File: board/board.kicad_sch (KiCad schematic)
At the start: 13 parts

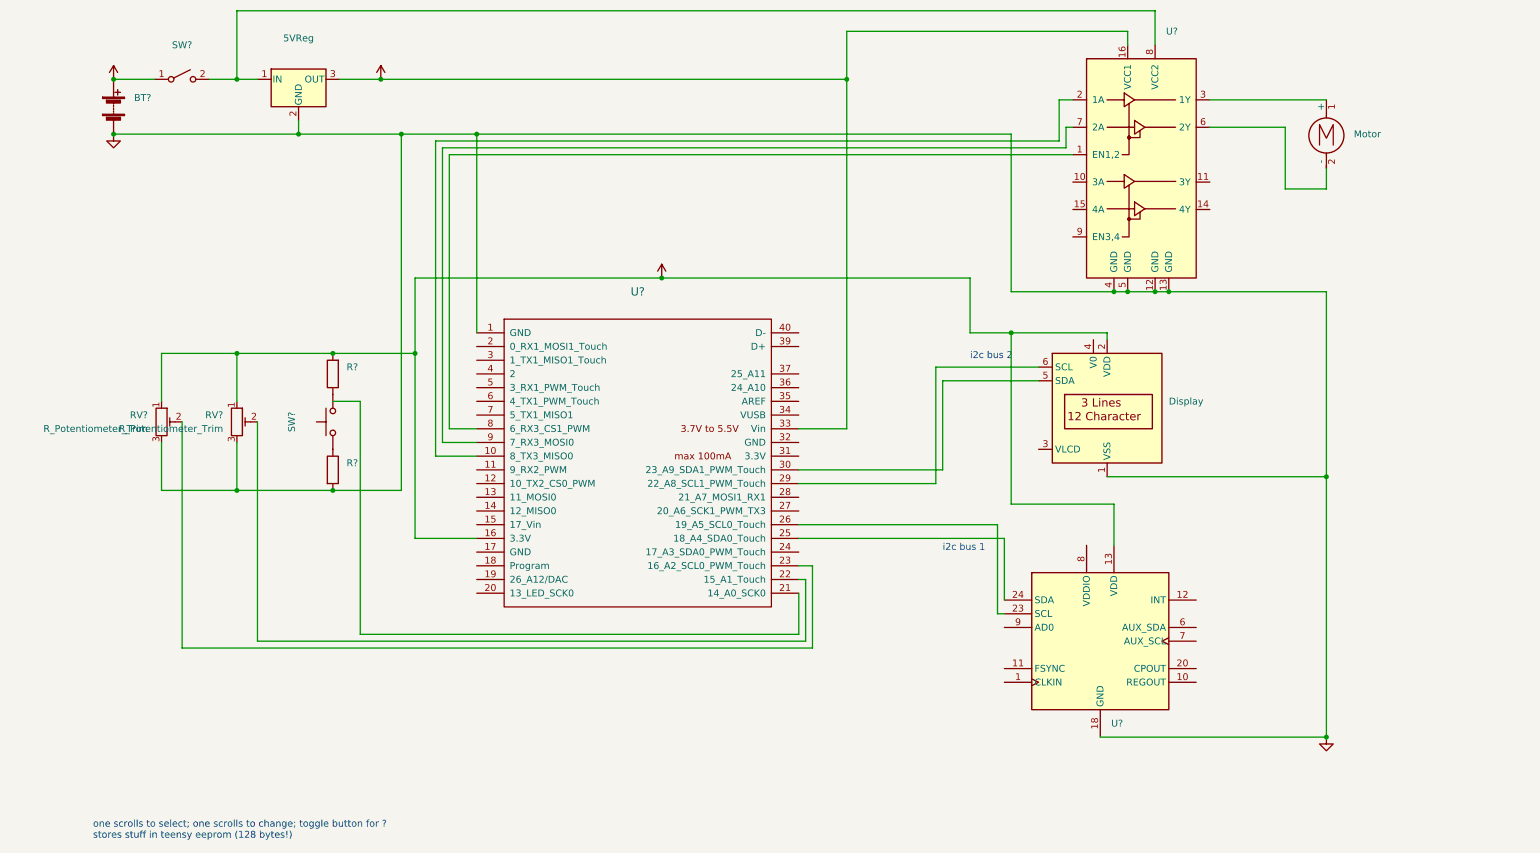
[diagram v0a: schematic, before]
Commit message: Schematic update to stepper
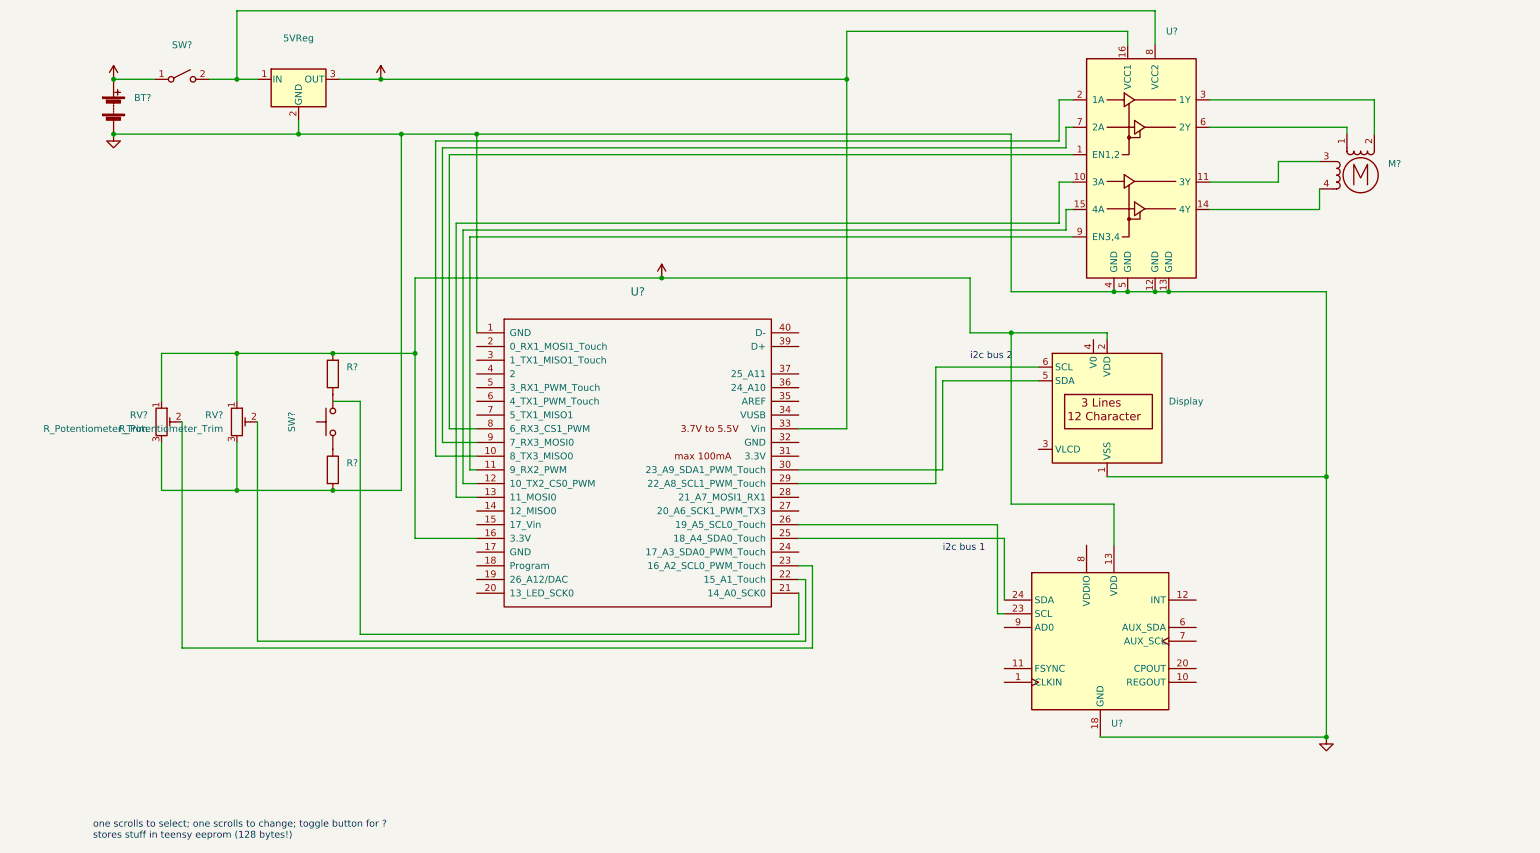
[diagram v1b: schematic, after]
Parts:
- removed Motor: (no value), symbol Motor:Motor_DC
- added M?: (no value), symbol Motor:Stepper_Motor_bipolar
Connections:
- net at U?.3 (1Y): now also M?.2 (-)
- net at U?.6 (2Y): now also M?.1
- net at U?.11 (9_RX2_PWM): now also U?.9 (EN3,4)
- net at U?.12 (10_TX2_CS0_PWM): now also U?.15 (4A)
- net at U?.13 (11_MOSI0): now also U?.10 (3A)
- net at U?.11 (3Y): now also M?.3
- net at U?.14 (4Y): now also M?.4
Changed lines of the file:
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@@
+    (stroke (width 0) (type default) (color 0 0 0 0))
+  )
+  (wire (pts (xy 256.54 33.02) (xy 256.54 39.37))
+    (stroke (width 0) (type default) (color 0 0 0 0))
+  )
+  (wire (pts (xy 226.06 38.1) (xy 251.46 38.1))
     (stroke (width 0) (type default) (color 0 0 0 0))
   )
@@
     (stroke (width 0) (type default) (color 0 0 0 0))
   )
-  (wire (pts (xy 226.06 33.02) (xy 247.65 33.02))
-    (stroke (width 0) (type default) (color 0 0 0 0))
-  )
   (wire (pts (xy 35.56 134.62) (xy 152.4 134.62))
     (stroke (width 0) (type default) (color 0 0 0 0))
   )
+  (wire (pts (xy 251.46 38.1) (xy 251.46 39.37))
+    (stroke (width 0) (type default) (color 0 0 0 0))
+  )
+  (wire (pts (xy 246.38 49.53) (xy 246.38 53.34))
+    (stroke (width 0) (type default) (color 0 0 0 0))
+  )
   (wire (pts (xy 152.4 134.62) (xy 152.4 119.38))
     (stroke (width 0) (type default) (color 0 0 0 0))
@@
     (stroke (width 0) (type default) (color 0 0 0 0))
   )
+  (wire (pts (xy 90.17 101.6) (xy 88.9 101.6))
+    (stroke (width 0) (type default) (color 0 0 0 0))
+  )
   (wire (pts (xy 85.09 43.18) (xy 200.66 43.18))
     (stroke (width 0) (type default) (color 0 0 0 0))
@@
     (stroke (width 0) (type default) (color 0 0 0 0))
   )
+  (wire (pts (xy 198.12 48.26) (xy 200.66 48.26))
+    (stroke (width 0) (type default) (color 0 0 0 0))
+  )
   (wire (pts (xy 151.13 121.92) (xy 151.13 133.35))
     (stroke (width 0) (type default) (color 0 0 0 0))
@@
     (stroke (width 0) (type default) (color 0 0 0 0))
   )
+  (wire (pts (xy 88.9 101.6) (xy 88.9 58.42))
+    (stroke (width 0) (type default) (color 0 0 0 0))
+  )
   (wire (pts (xy 82.55 40.64) (xy 198.12 40.64))
     (stroke (width 0) (type default) (color 0 0 0 0))
@@
     (stroke (width 0) (type default) (color 0 0 0 0))
   )
+  (wire (pts (xy 87.63 57.15) (xy 87.63 104.14))
+    (stroke (width 0) (type default) (color 0 0 0 0))
+  )
+  (wire (pts (xy 198.12 55.88) (xy 198.12 48.26))
+    (stroke (width 0) (type default) (color 0 0 0 0))
+  )
   (wire (pts (xy 57.15 36.83) (xy 57.15 39.37))
     (stroke (width 0) (type default) (color 0 0 0 0))
@@
     (stroke (width 0) (type default) (color 0 0 0 0))
   )
-  (wire (pts (xy 240.03 49.53) (xy 247.65 49.53))
+  (wire (pts (xy 86.36 55.88) (xy 198.12 55.88))
     (stroke (width 0) (type default) (color 0 0 0 0))
   )
@@
     (stroke (width 0) (type default) (color 0 0 0 0))
   )
-  (wire (pts (xy 226.06 38.1) (xy 240.03 38.1))
-    (stroke (width 0) (type default) (color 0 0 0 0))
-  )
   (wire (pts (xy 149.86 121.92) (xy 151.13 121.92))
     (stroke (width 0) (type default) (color 0 0 0 0))
@@
     (stroke (width 0) (type default) (color 0 0 0 0))
   )
+  (wire (pts (xy 226.06 48.26) (xy 238.76 48.26))
+    (stroke (width 0) (type default) (color 0 0 0 0))
+  )
   (wire (pts (xy 149.86 111.76) (xy 186.69 111.76))
     (stroke (width 0) (type default) (color 0 0 0 0))
   )
-  (wire (pts (xy 240.03 38.1) (xy 240.03 49.53))
-    (stroke (width 0) (type default) (color 0 0 0 0))
-  )
   (wire (pts (xy 90.17 39.37) (xy 189.23 39.37))
     (stroke (width 0) (type default) (color 0 0 0 0))
@@
     (stroke (width 0) (type default) (color 0 0 0 0))
   )
+  (wire (pts (xy 238.76 48.26) (xy 238.76 44.45))
+    (stroke (width 0) (type default) (color 0 0 0 0))
+  )
   (wire (pts (xy 208.28 68.58) (xy 210.82 68.58))
     (stroke (width 0) (type default) (color 0 0 0 0))
   )
+  (wire (pts (xy 86.36 106.68) (xy 86.36 55.88))
+    (stroke (width 0) (type default) (color 0 0 0 0))
+  )
   (wire (pts (xy 207.01 76.2) (xy 207.01 77.47))
     (stroke (width 0) (type default) (color 0 0 0 0))
@@
     (stroke (width 0) (type default) (color 0 0 0 0))
   )
+  (wire (pts (xy 199.39 57.15) (xy 87.63 57.15))
+    (stroke (width 0) (type default) (color 0 0 0 0))
+  )
   (wire (pts (xy 49.53 133.35) (xy 49.53 92.71))
     (stroke (width 0) (type default) (color 0 0 0 0))
@@
     (stroke (width 0) (type default) (color 0 0 0 0))
   )
+  (wire (pts (xy 200.66 53.34) (xy 199.39 53.34))
+    (stroke (width 0) (type default) (color 0 0 0 0))
+  )
   (wire (pts (xy 218.44 68.58) (xy 247.65 68.58))
     (stroke (width 0) (type default) (color 0 0 0 0))
@@
     (stroke (width 0) (type default) (color 0 0 0 0))
   )
+  (wire (pts (xy 226.06 33.02) (xy 256.54 33.02))
+    (stroke (width 0) (type default) (color 0 0 0 0))
+  )
   (wire (pts (xy 207.01 102.87) (xy 247.65 102.87))
     (stroke (width 0) (type default) (color 0 0 0 0))
@@
     (stroke (width 0) (type default) (color 0 0 0 0))
   )
+  (wire (pts (xy 238.76 44.45) (xy 246.38 44.45))
+    (stroke (width 0) (type default) (color 0 0 0 0))
+  )
   (wire (pts (xy 158.75 29.21) (xy 158.75 93.98))
     (stroke (width 0) (type default) (color 0 0 0 0))
@@
     (stroke (width 0) (type default) (color 0 0 0 0))
   )
-  (wire (pts (xy 247.65 49.53) (xy 247.65 45.72))
+  (wire (pts (xy 90.17 106.68) (xy 86.36 106.68))
+    (stroke (width 0) (type default) (color 0 0 0 0))
+  )
+  (wire (pts (xy 87.63 104.14) (xy 90.17 104.14))
     (stroke (width 0) (type default) (color 0 0 0 0))
   )
@@
     (stroke (width 0) (type default) (color 0 0 0 0))
   )
+  (wire (pts (xy 88.9 58.42) (xy 200.66 58.42))
+    (stroke (width 0) (type default) (color 0 0 0 0))
+  )
   (wire (pts (xy 181.61 76.2) (xy 189.23 76.2))
     (stroke (width 0) (type default) (color 0 0 0 0))
   )
+  (wire (pts (xy 199.39 53.34) (xy 199.39 57.15))
+    (stroke (width 0) (type default) (color 0 0 0 0))
+  )
   (wire (pts (xy 90.17 39.37) (xy 90.17 76.2))
     (stroke (width 0) (type default) (color 0 0 0 0))
   )
   (wire (pts (xy 189.23 68.58) (xy 208.28 68.58))
+    (stroke (width 0) (type default) (color 0 0 0 0))
+  )
+  (wire (pts (xy 246.38 53.34) (xy 226.06 53.34))
     (stroke (width 0) (type default) (color 0 0 0 0))
   )
@@
     (pin "3")
   )
-  (symbol (lib_id "Motor:Motor_DC") (at 247.65 38.1 0) (unit 1)
-    (in_bom yes) (on_board yes)
-    (property "Reference" "Motor" (id 0) (at 252.73 39.3699 0)
-      (effects (font (size 1.27 1.27)) (justify left))
-    )
-    (property "Value" "" (id 1) (at 252.73 41.9099 0)
-      (effects (font (size 1.27 1.27)) (justify left))
-    )
-    (property "Footprint" "" (id 2) (at 247.65 40.386 0)
-      (effects (font (size 1.27 1.27)) hide)
-    )
-    (property "Datasheet" "~" (id 3) (at 247.65 40.386 0)
-      (effects (font (size 1.27 1.27)) hide)
-    )
-    (pin "1")
-    (pin "2")
+  (symbol (lib_id "Motor:Stepper_Motor_bipolar") (at 254 46.99 0) (unit 1)
+    (in_bom yes) (on_board yes) (fields_autoplaced)
+    (property "Reference" "M?" (id 0) (at 259.08 44.869 0)
+      (effects (font (size 1.27 1.27)) (justify left))
+    )
+    (property "Value" "" (id 1) (at 259.08 47.409 0)
+      (effects (font (size 1.27 1.27)) (justify left))
+    )
+    (property "Footprint" "" (id 2) (at 254.254 47.244 0)
+      (effects (font (size 1.27 1.27)) hide)
+    )
+    (property "Datasheet" "http://www.infineon.com/dgdl/Application-Note-TLE8110EE_driving_UniPolarStepperMotor_V1.1.pdf?fileId=db3a30431be39b97011be5d0aa0a00b0" (id 3) (at 254.254 47.244 0)
+      (effects (font (size 1.27 1.27)) hide)
+    )
+    (pin "1")
+    (pin "2")
+    (pin "3")
+    (pin "4")
   )
   (symbol (lib_id "power:GND") (at 22.86 39.37 0) (unit 1)
@@
       (reference "Display") (unit 1) (value "not exactly this") (footprint "Display:EA_T123X-I2C")
     )
-    (path "/1e750dc4-ea9e-4bf8-b3d1-19245103338e"
-      (reference "Motor") (unit 1) (value "Motor_DC") (footprint "")
+    (path "/1a2326e8-a713-4b21-bd05-c054d5019aad"
+      (reference "M?") (unit 1) (value "Stepper_Motor_bipolar") (footprint "")
     )
     (path "/41a6e2d3-e37e-405b-98da-024be97c5764"

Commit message: Check in state before computer move
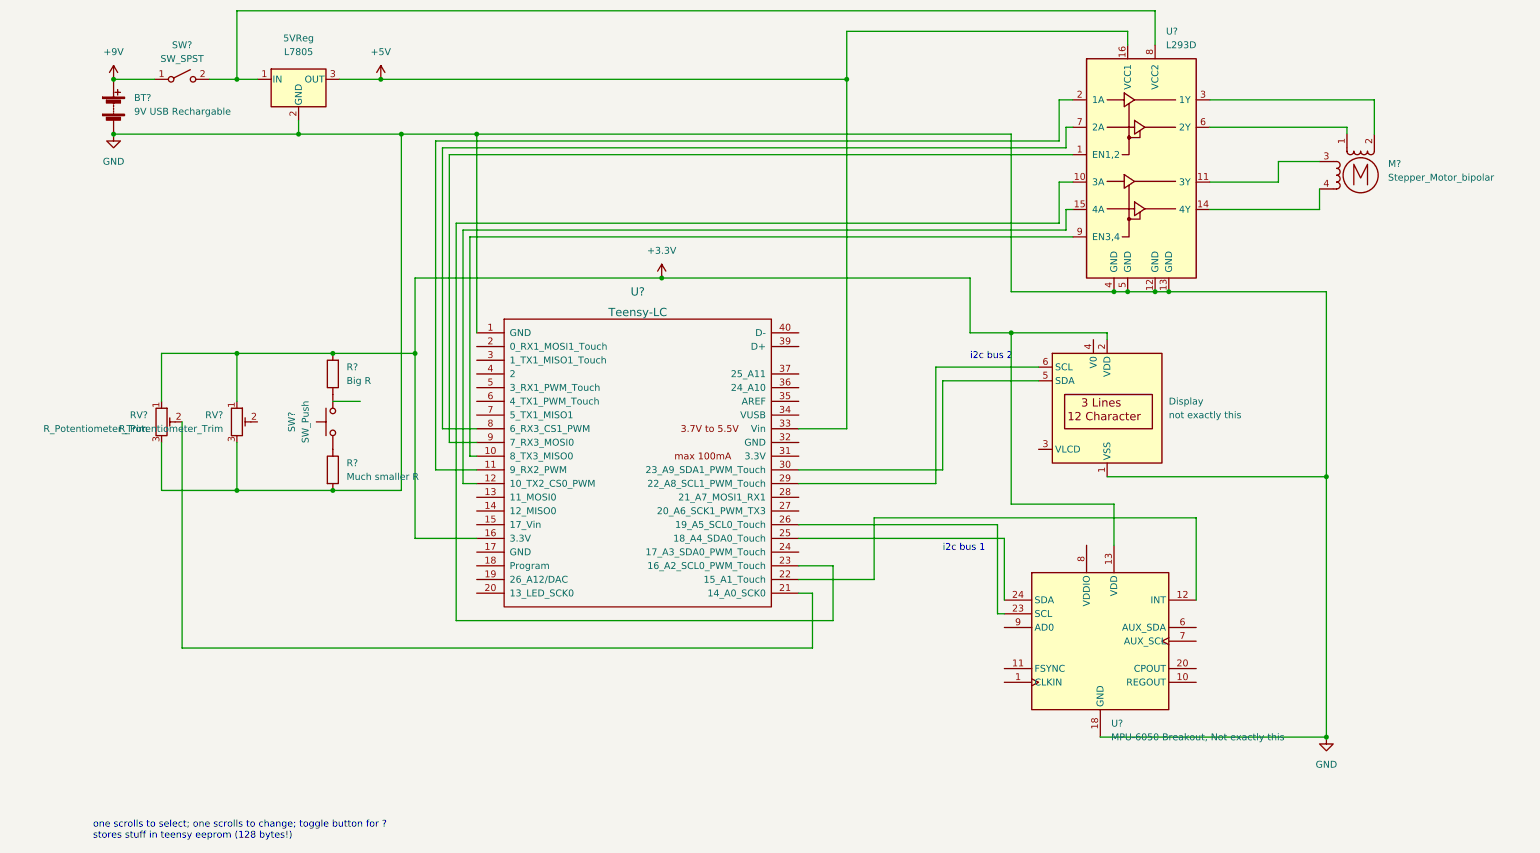
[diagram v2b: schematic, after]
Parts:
- 5VReg: value (none) -> L7805
- BT?: value (none) -> 9V USB Rechargable
- Display: value (none) -> not exactly this; footprint (none) -> Display:EA_T123X-I2C
- M?: value (none) -> Stepper_Motor_bipolar
- R?: value (none) -> Big R
- R?: value (none) -> Much smaller R
- SW?: value (none) -> SW_Push
- SW?: value (none) -> SW_SPST
- U?: value (none) -> MPU-6050 Breakout, Not exactly this; footprint (none) -> Sensor_Motion:InvenSense_QFN-24_4x4mm_P0.5mm
- U?: value (none) -> Teensy-LC
- U?: value (none) -> L293D; footprint (none) -> Package_DIP:DIP-16_W7.62mm
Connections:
- net at RV?.2: no longer U?.22 (15_A1_Touch)
- net at U?.12 (INT): now also U?.22 (15_A1_Touch)
- net at RV?.2: now also U?.21 (14_A0_SCK0); no longer U?.23 (16_A2_SCL0_PWM_Touch)
- net at U?.10 (8_TX3_MISO0): now also U?.9 (EN3,4); no longer U?.2 (1A)
- net at U?.11 (9_RX2_PWM): now also U?.2 (1A); no longer U?.9 (EN3,4)
- net at U?.13 (11_MOSI0): no longer U?.10 (3A)
- net at U?.8 (6_RX3_CS1_PWM): now also U?.7 (2A); no longer U?.1 (EN1,2)
- net at U?.9 (7_RX3_MOSI0): now also U?.1 (EN1,2); no longer U?.7 (2A)
- new net: U?.10 (3A), U?.23 (16_A2_SCL0_PWM_Touch)
